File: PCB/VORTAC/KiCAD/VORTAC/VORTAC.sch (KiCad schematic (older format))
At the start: 0 parts

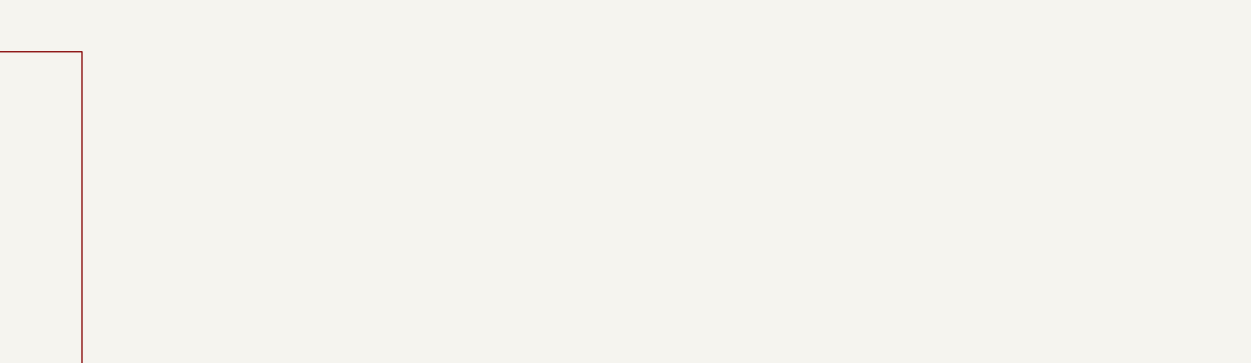
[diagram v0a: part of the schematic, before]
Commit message: pcb, step and headers
-headers schematic updated
-created rough pcb placement of headers
-created step file for inspection in fusion 360
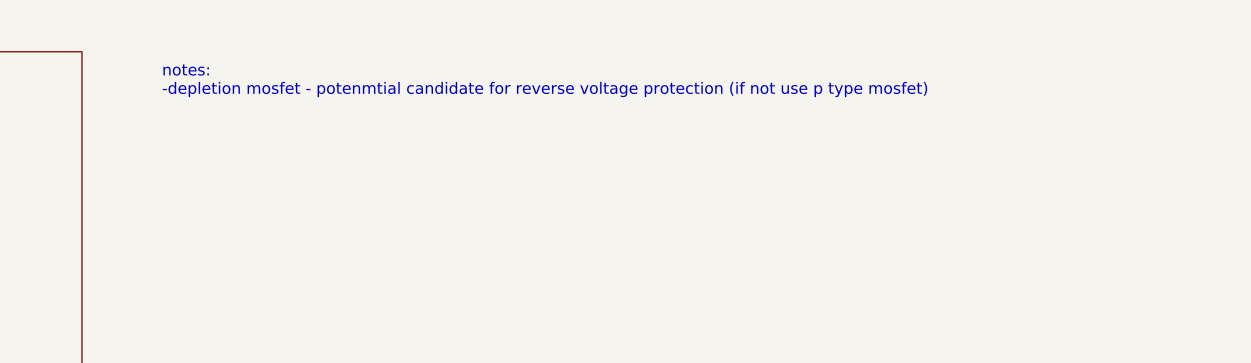
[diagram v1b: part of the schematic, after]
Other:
- note added: "notes:\n-depletion mosfet - potenmtial candidate for reverse voltage protection (if not use p type mosfet)"
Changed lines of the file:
@@
 F1 "MCU.sch" 79
 $EndSheet
+Text Notes 6850 1050 0    50   ~ 0
+notes:\n-depletion mosfet - potenmtial candidate for reverse voltage protection (if not use p type mosfet)
 $EndSCHEMATC
